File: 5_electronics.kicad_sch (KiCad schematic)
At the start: 0 parts

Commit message: Add gpio pins
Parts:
- added J1: Conn_02x20_Odd_Even, symbol Connector_Generic:Conn_02x20_Odd_Even
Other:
- title: (none) -> Smart Camera System
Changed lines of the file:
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@@
 	(generator_version "9.0")
 	(paper "A4")
+	(title_block
+		(title "Smart Camera System")
+		(date "2026-04-26")
+		(rev "A")
+	)
+	(label "GPIO EXPANSION"
+		(at 31.75 160.02 0)
+		(effects
+			(font
+				(size 1.27 1.27)
+			)
+			(justify left bottom)
+		)
+	)
+	(label "J1 – Raspberry Pi 4 GPIO"
+		(at 29.21 95.25 0)
+		(effects
+			(font
+				(size 1.27 1.27)
+			)
+			(justify left bottom)
+		)
+	)
+	(symbol
+		(lib_id "Connector_Generic:Conn_02x20_Odd_Even")
+		(at 36.83 123.19 0)
+		(unit 1)
+		(exclude_from_sim no)
+		(in_bom yes)
+		(on_board yes)
+		(dnp no)
+		(fields_autoplaced yes)
+		(property "Reference" "J1"
+			(at 38.1 93.98 0)
+			(effects
+				(font
+					(size 1.27 1.27)
+				)
+				(hide yes)
+			)
+		)
+		(property "Value" "Conn_02x20_Odd_Even"
+			(at 38.1 96.52 0)
+			(effects
+				(font
+					(size 1.27 1.27)
+				)
+				(hide yes)
+			)
+		)
+		(property "Footprint" ""
+			(at 36.83 123.19 0)
+			(effects
+				(font
+					(size 1.27 1.27)
+				)
+				(hide yes)
+			)
+		)
+		(property "Datasheet" "~"
+			(at 36.83 123.19 0)
+			(effects
+				(font
+					(size 1.27 1.27)
+				)
+				(hide yes)
+			)
+		)
+		(property "Description" "Generic connector, double row, 02x20, odd/even pin numbering scheme (row 1 odd numbers, row 2 even numbers), script generated (kicad-library-utils/schlib/autogen/connector/)"
+			(at 36.83 123.19 0)
+			(effects
+				(font
+					(size 1.27 1.27)
+				)
+				(hide yes)
+			)
+		)
+		(pin "39"
+		)
+		(pin "2"
+		)
+		(pin "37"
+		)
+		(pin "35"
+		)
+		(pin "33"
+		)
+		(pin "17"
+		)
+		(pin "25"
+		)
+		(pin "23"
+		)
+		(pin "21"
+		)
+		(pin "19"
+		)
+		(pin "27"
+		)
+		(pin "5"
+		)
+		(pin "9"
+		)
+		(pin "7"
+		)
+		(pin "1"
+		)
+		(pin "3"
+		)
+		(pin "29"
+		)
+		(pin "15"
+		)
+		(pin "13"
+		)
+		(pin "11"
+		)
+		(pin "31"
+		)
+		(pin "12"
+		)
+		(pin "16"
+		)
+		(pin "14"
+		)
+		(pin "22"
+		)
+		(pin "24"
+		)
+		(pin "18"
+		)
+		(pin "30"
+		)
+		(pin "20"
+		)
+		(pin "32"
+		)
+		(pin "26"
+		)
+		(pin "38"
+		)
+		(pin "28"
+		)
+		(pin "40"
+		)
+		(pin "34"
+		)
+		(pin "36"
+		)
+		(pin "4"
+		)
+		(pin "6"
+		)
+		(pin "8"
+		)
+		(pin "10"
+		)
+		(instances
+			(project "5_electronics"
+				(path "/b9f81094-eb83-479c-a644-7dc92c1427a8"
+					(reference "J1")
+					(unit 1)
+				)
+			)
+		)
+	)
 	(sheet_instances
 		(path "/"

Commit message: Update page setting
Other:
- title: Smart Camera System -> Raspberry Pi 4 Module B
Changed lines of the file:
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@@
 	(paper "A4")
 	(title_block
-		(title "Smart Camera System")
+		(title "Raspberry Pi 4 Module B")
 		(date "2026-04-26")
 		(rev "A")

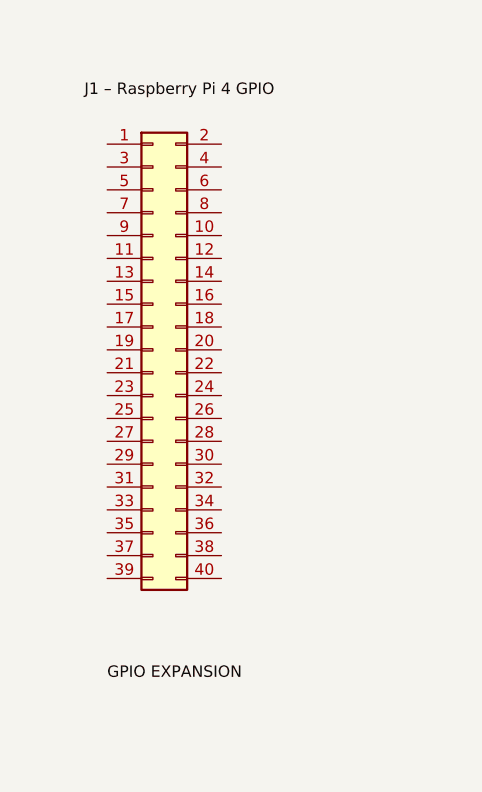
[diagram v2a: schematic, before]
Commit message: Update gpio pins
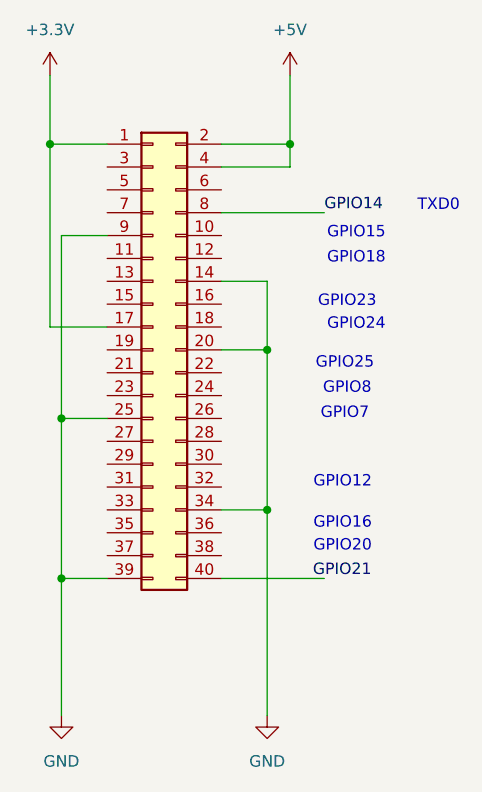
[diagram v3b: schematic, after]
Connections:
- net +3.3V: now reaches J1.1 (Pin_1)
- net +3.3V: now also J1.17 (Pin_17)
- net GND: now reaches J1.14 (Pin_14)
- net GND: now also J1.20 (Pin_20), J1.25 (Pin_25), J1.34 (Pin_34), J1.39 (Pin_39), J1.9 (Pin_9)
- net +5V: now reaches J1.2 (Pin_2)
- net +5V: now also J1.4 (Pin_4)
- net at J1.40 (Pin_40): no longer names the net of J1.40 (Pin_40)
- net GPIO14: now reaches J1.8 (Pin_8)
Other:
- note added: "GPIO12"
- note added: "GPIO15"
- note added: "GPIO16"
- note added: "GPIO18"
- note added: "GPIO20"
- note added: "GPIO23"
- note added: "GPIO24"
- note added: "GPIO25"
- note added: "GPIO7"
- note added: "GPIO8"
- note added: "TXD0"

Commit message: Update gpio pins
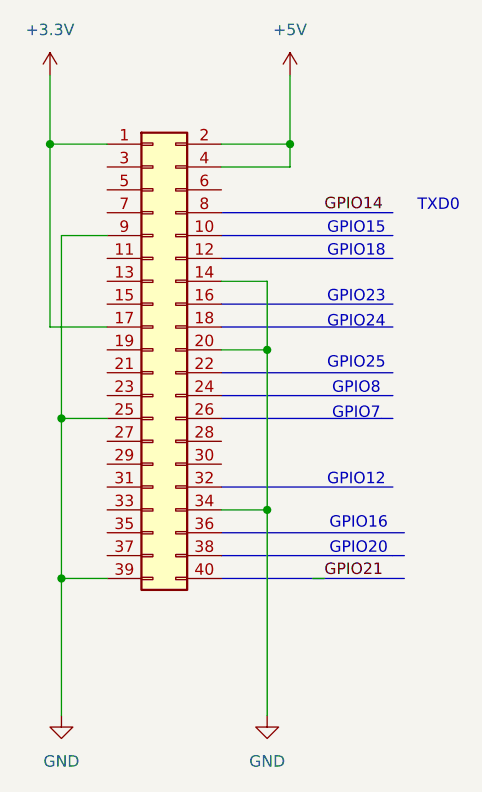
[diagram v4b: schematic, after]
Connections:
- net GPIO14: no longer J1.8 (Pin_8)
- net at J1.40 (Pin_40): no longer names the net of J1.40 (Pin_40)
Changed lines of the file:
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@@
 	(text "GPIO24"
 		(exclude_from_sim no)
-		(at 59.436 120.396 0)
+		(at 59.436 120.142 0)
 		(effects
 			(font
@@
 	(text "GPIO15"
 		(exclude_from_sim no)
-		(at 59.436 110.236 0)
+		(at 59.436 109.728 0)
 		(effects
 			(font
@@
 	(text "GPIO18\n"
 		(exclude_from_sim no)
-		(at 59.436 113.03 0)
+		(at 59.436 112.268 0)
 		(effects
 			(font
@@
 	(text "GPIO16"
 		(exclude_from_sim no)
-		(at 57.912 142.494 0)
+		(at 59.69 142.494 0)
 		(effects
 			(font
@@
 	(text "GPIO20\n"
 		(exclude_from_sim no)
-		(at 57.912 145.034 0)
+		(at 59.69 145.288 0)
 		(effects
 			(font
@@
 	(text "GPIO23"
 		(exclude_from_sim no)
-		(at 58.42 117.856 0)
+		(at 59.436 117.348 0)
 		(effects
 			(font
@@
 	(text "GPIO7"
 		(exclude_from_sim no)
-		(at 58.166 130.302 0)
+		(at 59.436 130.302 0)
 		(effects
 			(font
@@
 	(text "GPIO25"
 		(exclude_from_sim no)
-		(at 58.166 124.714 0)
+		(at 59.436 124.714 0)
 		(effects
 			(font
@@
 	(text "GPIO8\n"
 		(exclude_from_sim no)
-		(at 58.42 127.508 0)
+		(at 59.436 127.508 0)
 		(effects
 			(font
@@
 	(text "GPIO12"
 		(exclude_from_sim no)
-		(at 57.912 137.922 0)
+		(at 59.436 137.668 0)
 		(effects
 			(font
@@
 	(wire
 		(pts
+			(xy 55.88 148.59) (xy 54.61 148.59)
+		)
+		(stroke
+			(width 0)
+			(type default)
+		)
+	)
+	(wire
+		(pts
 			(xy 52.07 100.33) (xy 44.45 100.33)
 		)
@@
 		)
 	)
+	(polyline
+		(pts
+			(xy 62.23 130.81) (xy 63.5 130.81)
+		)
+		(stroke
+			(width 0)
+			(type default)
+		)
+	)
+	(polyline
+		(pts
+			(xy 44.45 113.03) (xy 63.5 113.03)
+		)
+		(stroke
+			(width 0)
+			(type default)
+		)
+	)
+	(polyline
+		(pts
+			(xy 44.45 107.95) (xy 63.5 107.95)
+		)
+		(stroke
+			(width 0)
+			(type default)
+		)
+	)
+	(polyline
+		(pts
+			(xy 44.45 120.65) (xy 63.5 120.65)
+		)
+		(stroke
+			(width 0)
+			(type default)
+		)
+	)
 	(wire
 		(pts
@@
 		)
 	)
+	(polyline
+		(pts
+			(xy 44.45 146.05) (xy 63.5 146.05)
+		)
+		(stroke
+			(width 0)
+			(type default)
+		)
+	)
+	(polyline
+		(pts
+			(xy 44.45 110.49) (xy 63.5 110.49)
+		)
+		(stroke
+			(width 0)
+			(type default)
+		)
+	)
 	(wire
 		(pts
@@
 		)
 	)
+	(polyline
+		(pts
+			(xy 44.45 125.73) (xy 63.5 125.73)
+		)
+		(stroke
+			(width 0)
+			(type default)
+		)
+	)
 	(wire
 		(pts
@@
 		)
 	)
+	(polyline
+		(pts
+			(xy 44.45 143.51) (xy 64.77 143.51)
+		)
+		(stroke
+			(width 0)
+			(type default)
+		)
+	)
+	(polyline
+		(pts
+			(xy 44.45 128.27) (xy 63.5 128.27)
+		)
+		(stroke
+			(width 0)
+			(type default)
+		)
+	)
 	(wire
 		(pts
@@
 		)
 	)
+	(polyline
+		(pts
+			(xy 44.45 148.59) (xy 64.77 148.59)
+		)
+		(stroke
+			(width 0)
+			(type default)
+		)
+	)
 	(wire
 		(pts
@@
 		)
 	)
+	(polyline
+		(pts
+			(xy 44.45 130.81) (xy 62.23 130.81)
+		)
+		(stroke
+			(width 0)
+			(type default)
+		)
+	)
 	(wire
 		(pts
@@
 		)
 	)
-	(wire
-		(pts
-			(xy 44.45 107.95) (xy 55.88 107.95)
-		)
-		(stroke
-			(width 0)
-			(type default)
-		)
-	)
-	(wire
-		(pts
-			(xy 44.45 148.59) (xy 55.88 148.59)
+	(polyline
+		(pts
+			(xy 44.45 118.11) (xy 63.5 118.11)
 		)
 		(stroke
@@
 		(pts
 			(xy 44.45 102.87) (xy 52.07 102.87)
+		)
+		(stroke
+			(width 0)
+			(type default)
+		)
+	)
+	(polyline
+		(pts
+			(xy 63.5 146.05) (xy 64.77 146.05)
+		)
+		(stroke
+			(width 0)
+			(type default)
+		)
+	)
+	(polyline
+		(pts
+			(xy 44.45 138.43) (xy 63.5 138.43)
 		)
 		(stroke
@@
 	)
 	(label "GPIO21"
-		(at 54.61 148.59 0)
-		(effects
-			(font
+		(at 55.88 148.59 0)
+		(effects
+			(font
